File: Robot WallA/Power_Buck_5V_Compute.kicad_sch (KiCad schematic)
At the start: 19 parts, among them Q1 BSS138, U10 PTN78060W_EUW-7

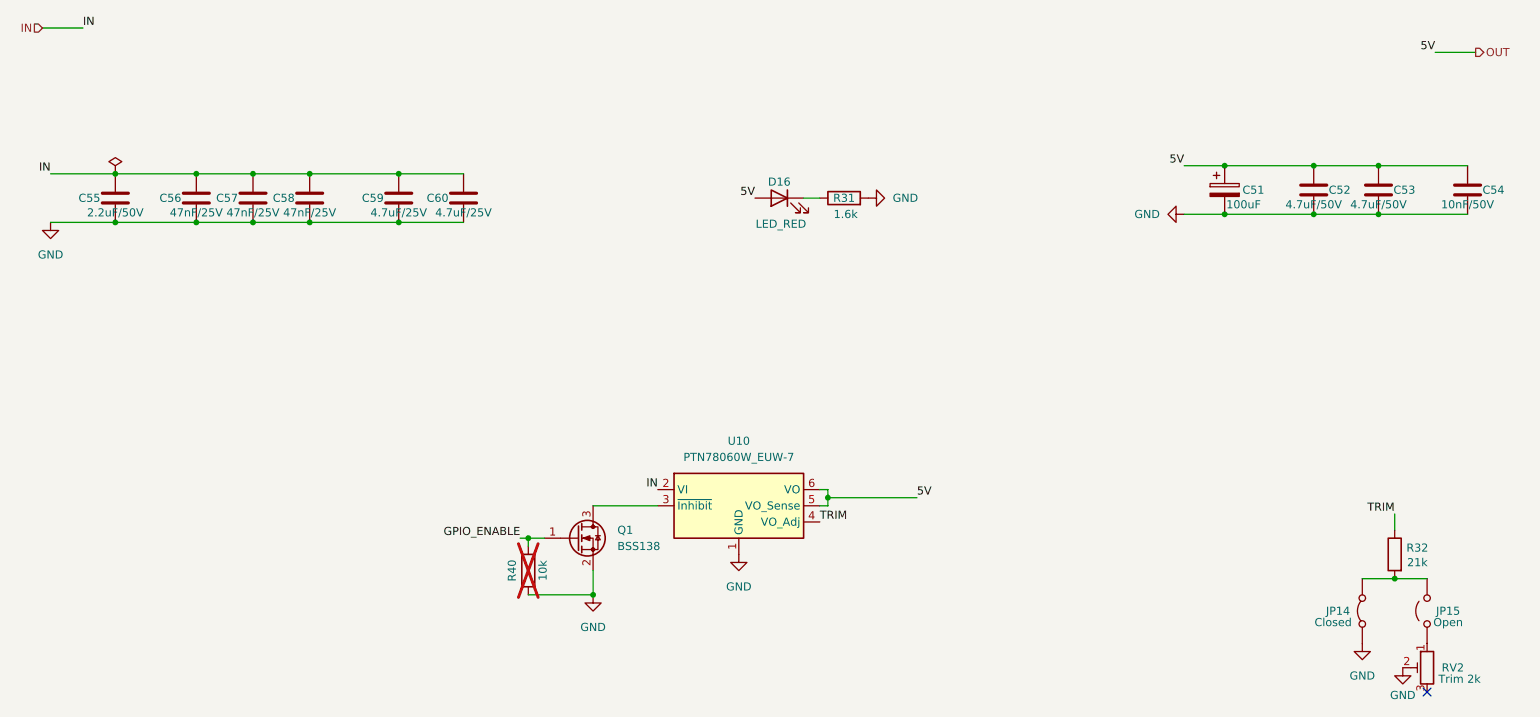
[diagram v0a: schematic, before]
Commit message: Added diode for Type-C connector in case we accidentally power the board with this connector.
Updated fab files
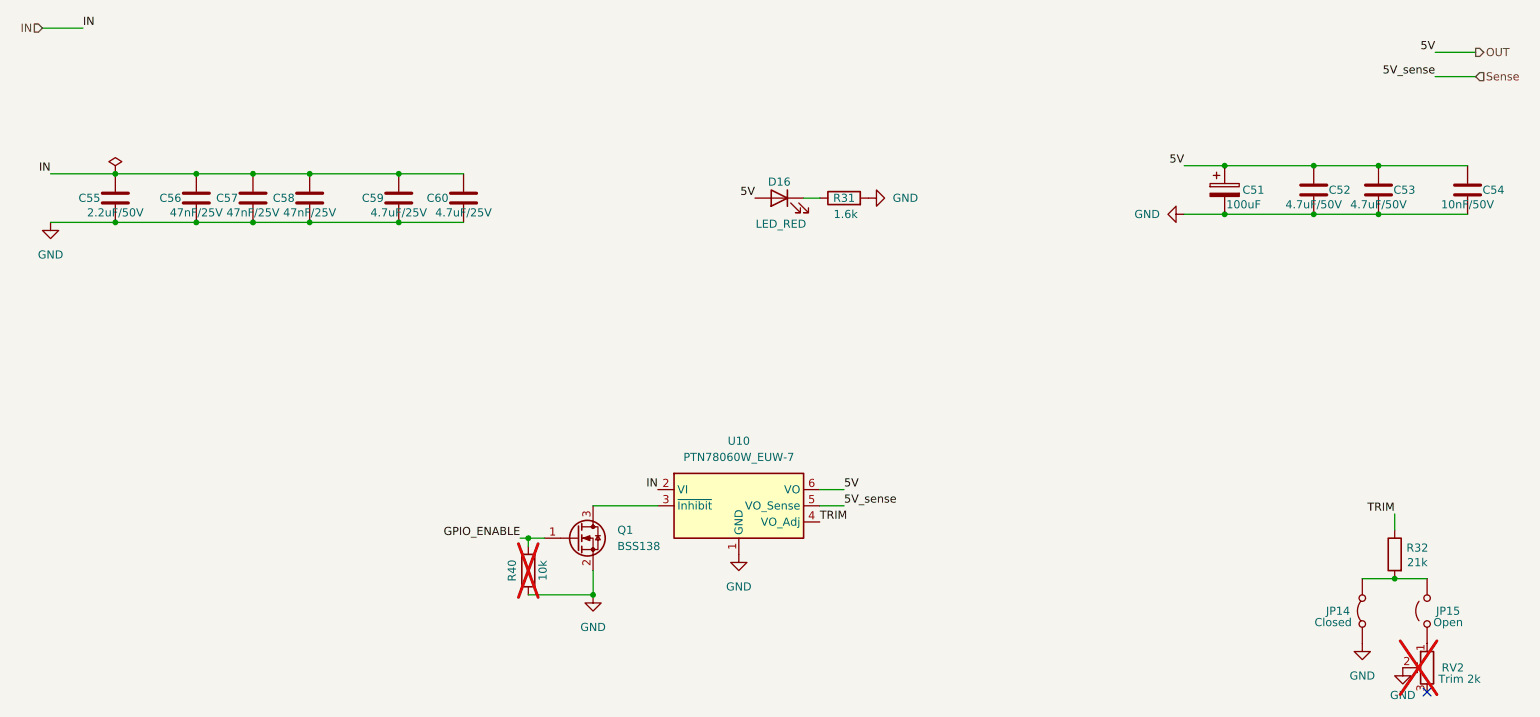
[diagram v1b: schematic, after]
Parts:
- RV2: now not fitted
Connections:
- net OUT: no longer U10.5 (VO_Sense)
- new net Sense: U10.5 (VO_Sense)
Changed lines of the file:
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@@
-	)
-	(junction
-		(at 162.56 99.06)
-		(diameter 0)
-		(color 0 0 0 0)
 	)
 	(junction
@@
 	(wire
 		(pts
+			(xy 257.81 33.02) (xy 264.16 33.02)
+		)
+		(stroke
+			(width 0)
+			(type default)
+		)
+	)
+	(wire
+		(pts
 			(xy 248.92 54.61) (xy 262.89 54.61)
 		)
@@
 	(wire
 		(pts
-			(xy 161.29 100.33) (xy 162.56 100.33)
+			(xy 161.29 100.33) (xy 165.1 100.33)
 		)
 		(stroke
@@
 	(wire
 		(pts
-			(xy 162.56 99.06) (xy 162.56 97.79)
-		)
-		(stroke
-			(width 0)
-			(type default)
-		)
-	)
-	(wire
-		(pts
-			(xy 162.56 99.06) (xy 176.53 99.06)
-		)
-		(stroke
-			(width 0)
-			(type default)
-		)
-	)
-	(wire
-		(pts
 			(xy 238.76 46.99) (xy 248.92 46.99)
 		)
@@
 	(wire
 		(pts
-			(xy 162.56 97.79) (xy 161.29 97.79)
+			(xy 161.29 97.79) (xy 165.1 97.79)
 		)
 		(stroke
@@
 		(pts
 			(xy 40.64 48.26) (xy 50.8 48.26)
-		)
-		(stroke
-			(width 0)
-			(type default)
-		)
-	)
-	(wire
-		(pts
-			(xy 162.56 100.33) (xy 162.56 99.06)
 		)
 		(stroke
@@
 		)
 	)
+	(label "5V_sense"
+		(at 257.81 33.02 180)
+		(effects
+			(font
+				(size 1.27 1.27)
+			)
+			(justify right bottom)
+		)
+	)
 	(label "IN"
 		(at 40.64 48.26 180)
@@
 		)
 	)
+	(label "5V_sense"
+		(at 165.1 100.33 0)
+		(effects
+			(font
+				(size 1.27 1.27)
+			)
+			(justify left bottom)
+		)
+	)
 	(label "IN"
 		(at 135.89 97.79 180)
@@
 	)
 	(label "5V"
-		(at 176.53 99.06 0)
+		(at 165.1 97.79 0)
 		(effects
 			(font
@@
 		(shape output)
 		(at 264.16 29.21 0)
+		(effects
+			(font
+				(size 1.27 1.27)
+			)
+			(justify left)
+		)
+	)
+	(hierarchical_label "Sense"
+		(shape input)
+		(at 264.16 33.02 0)
 		(effects
 			(font
@@
 		(in_bom yes)
 		(on_board yes)
-		(dnp no)
+		(dnp yes)
 		(property "Reference" "RV2"
 			(at 258.826 125.73 0)

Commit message: Modified footprint to simplify BOM. Finalized BOM.
Updated fab files
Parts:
- C51: Manufacturer_Part_Number (none) -> EEU-FC1V101
- C54: Manufacturer_Part_Number (none) -> CL21B103KBANNNC
- C56, C57, C58: value 47nF/25V -> 47nF/50V; Manufacturer_Part_Number (none) -> CC0603KPX7R9BB473
- C59, C60: value 4.7uF/25V -> 4.7uF/50V
- JP14: now left out of the parts list
- R31: Manufacturer_Part_Number (none) -> ERJ-3EKF1601V
- R32: Manufacturer_Part_Number (none) -> RC0603FR-0721KL
- R40: Manufacturer_Part_Number (none) -> 667-ERJ-3GEYJ103V

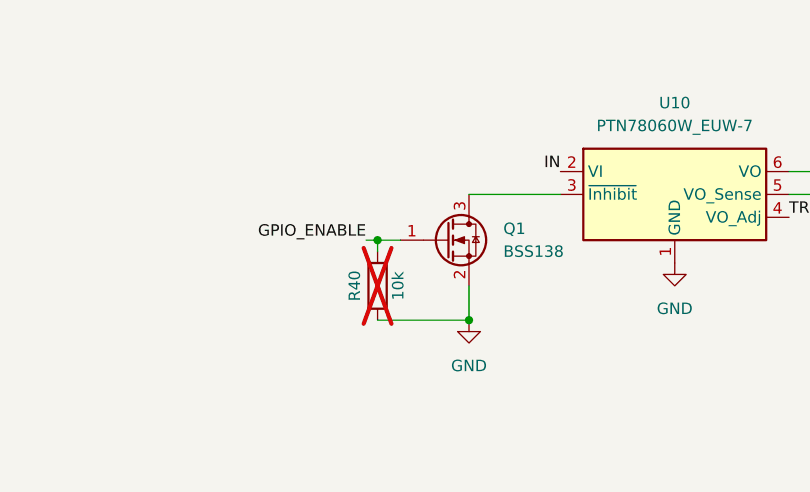
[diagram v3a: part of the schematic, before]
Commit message: Corrected schematic labels encoders according to PCB labels... (inversion...)
Add fab files
cleaned
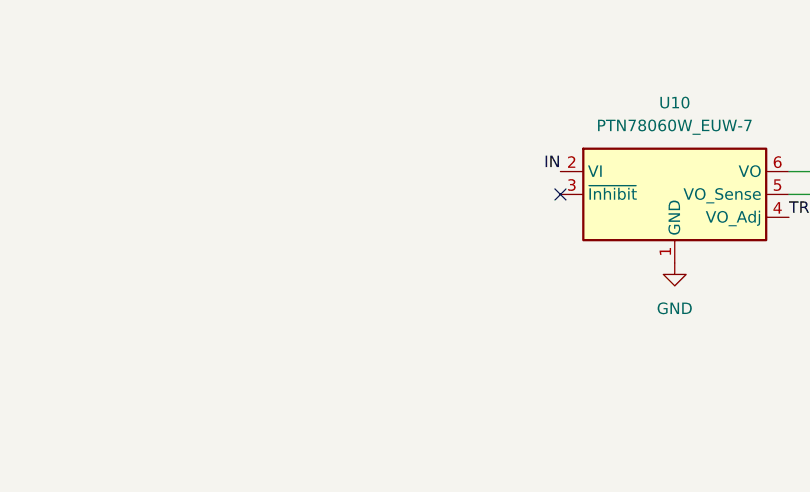
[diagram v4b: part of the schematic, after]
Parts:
- removed Q1: BSS138, Package_TO_SOT_SMD:SOT-23, symbol Transistor_FET:BSS138
- removed R40: 10k, Resistor_SMD:R_0603_1608Metric_Pad0.98x0.95mm_HandSolder, symbol Device:R
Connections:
- no-connect marks 1 -> 2
